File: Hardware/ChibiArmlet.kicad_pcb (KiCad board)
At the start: 2 copper layers, 8 x 8 mm, 52 parts, among them Q2 MMBT2222, Q3 LED_RGB 5050

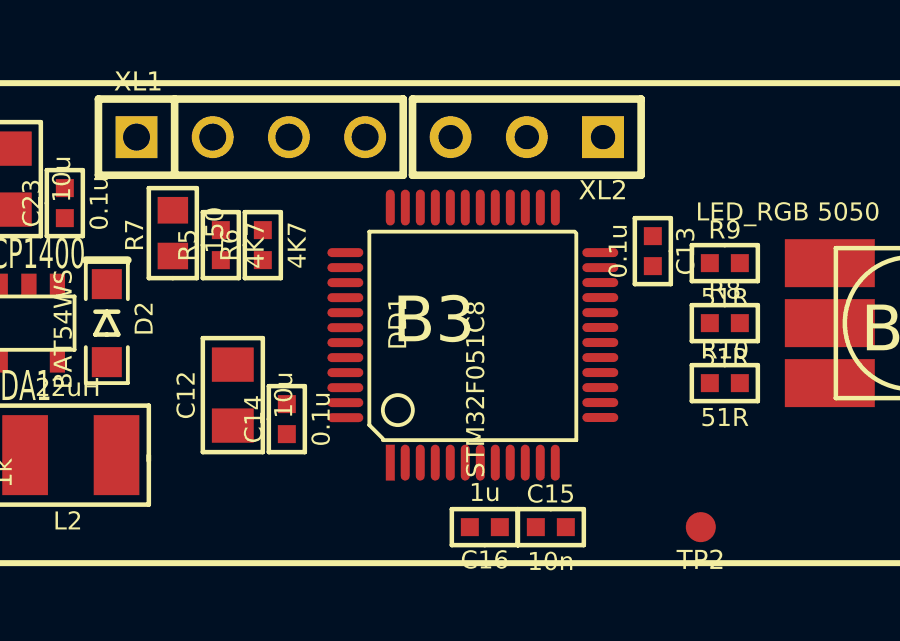
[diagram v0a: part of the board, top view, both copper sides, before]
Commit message: MCU replaced with stm32L100c6
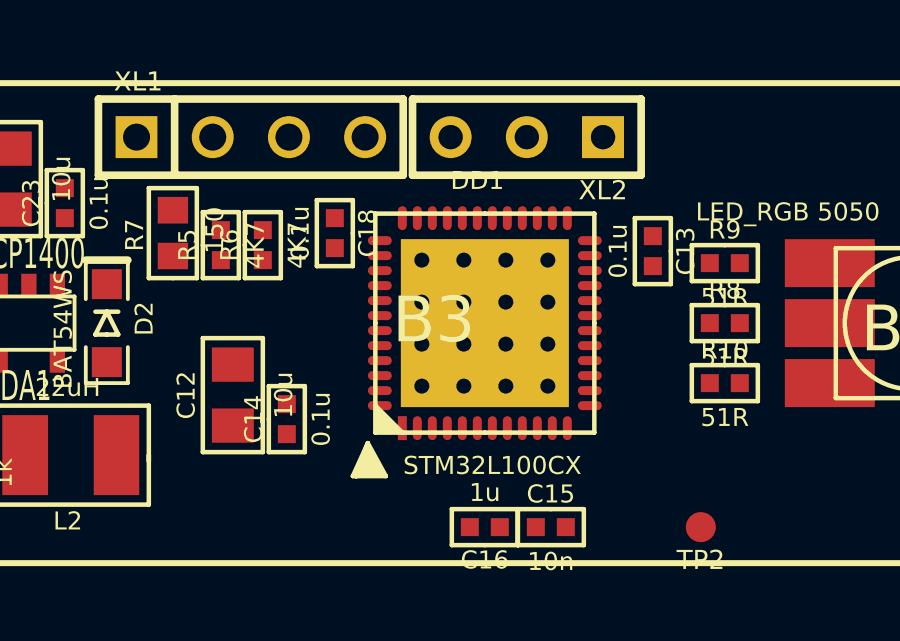
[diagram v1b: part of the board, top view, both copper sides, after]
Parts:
- added C18: 0.1u, CAP_0402, F.Cu at (197.0, 178.0)
- DD1: value STM32F051C8 -> STM32L100CX; footprint LQFP48 -> QFN48
- moved DD1 0.57 mm to (202.0, 181.0), turned to 0 degrees
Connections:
- DD1 pad 1: +3.3V -> (no net)
- DD1 pad 10: (no net) -> N-0000020
- DD1 pad 11: N-000001 (its old number) -> (no net)
- DD1 pad 21: (no net) -> /Buzzer
- DD1 pad 35: (no net) -> GND
- DD1 pad 36: (no net) -> +3.3V
- DD1 pad 40: /GREEN_LED -> (no net)
- DD1 pad 41: /PeriphPwr -> /GREEN_LED
- DD1 pad 42: /P_SCL -> (no net)
- DD1 pad 43: /P_SDA -> /PeriphPwr
- DD1 pad 45: /Buzzer -> /P_SCL
- DD1 pad 46: (no net) -> /P_SDA
- R1 pad 1: N-000001 (its old number) -> N-0000020

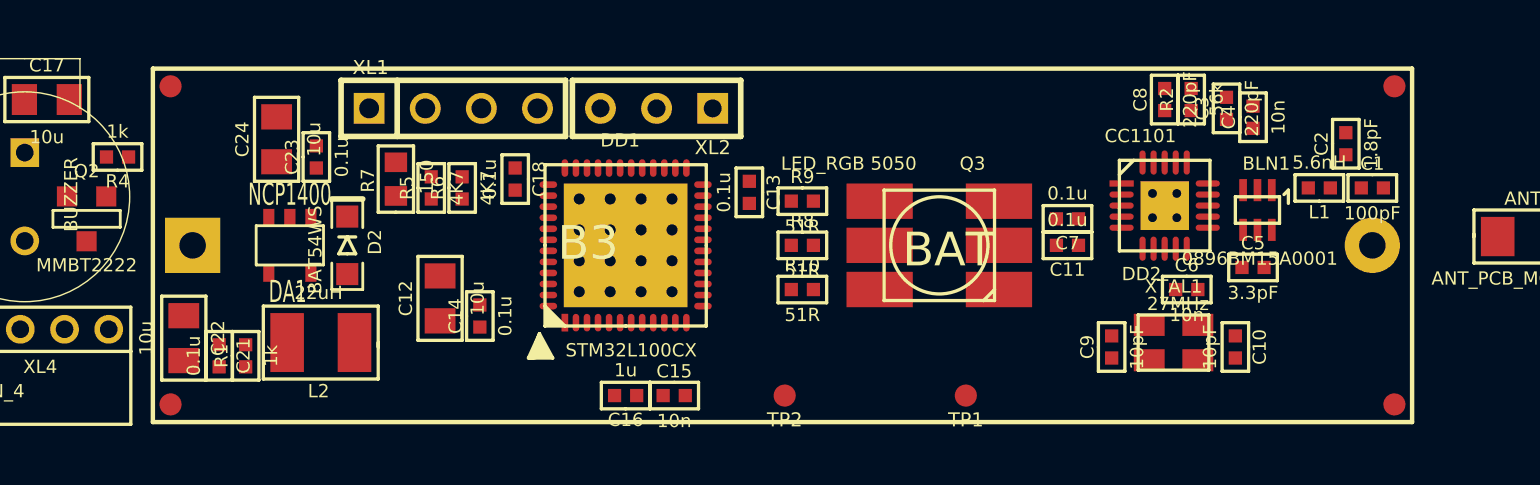
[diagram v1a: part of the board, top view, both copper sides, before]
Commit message: Again, buttons and display added.
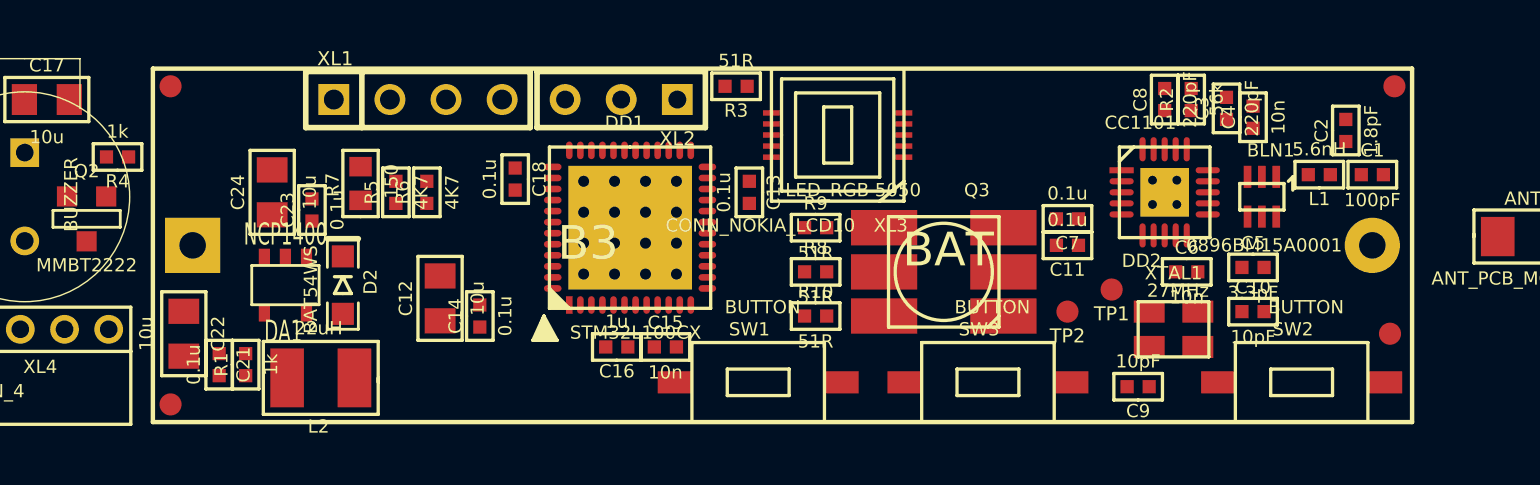
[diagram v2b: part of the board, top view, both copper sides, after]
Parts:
- added R3: 51R, RES_0402, F.Cu at (207.0, 173.8)
- added SW1: BUTTON, BUTTON_IT1181A, F.Cu at (208.0, 187.2)
- added SW2: BUTTON, BUTTON_IT1181A, F.Cu at (232.6, 187.2)
- added SW3: BUTTON, BUTTON_IT1181A, F.Cu at (218.4, 187.2)
- added XL3: CONN_NOKIA_LCD10, CONN_NOKIA_LCD, F.Cu at (211.6, 176.0)
- moved TP2 13.4 mm to (222.0, 184.0)
- moved TP1 8.16 mm to (224.0, 183.0)
- moved RP1 3.21 mm to (236.6, 185.0)
- moved C23 2.41 mm to (187.8, 179.4)
- moved C24 2.41 mm to (186.0, 178.6)
- moved C16 2.24 mm to (201.6, 185.6)
- moved C15 2.24 mm to (203.8, 185.6)
- moved C9 2.16 mm to (225.2, 187.4), turned to 180 degrees
- moved D2 1.81 mm to (189.2, 182.8)
- moved DA1 1.81 mm to (186.6, 182.8)
- moved C10 1.79 mm to (230.4, 184.0), turned to 0 degrees
- moved XL1 1.65 mm to (192.6, 174.4)
- moved XL2 1.65 mm to (201.8, 174.4)
- moved R5 1.61 mm to (191.6, 178.6)
- moved R6 1.61 mm to (193.0, 178.6)
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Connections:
- DD1 pad 11: (no net) -> /BTN1
- DD1 pad 20: (no net) -> /BTN2
- DD1 pad 21: /Buzzer -> /LCD_SDA
- DD1 pad 22: (no net) -> /LCD_XRES
- DD1 pad 25: (no net) -> /LCD_SCLK
- DD1 pad 26: (no net) -> /LCD_XCS
- DD1 pad 27: (no net) -> /LCD_BCKLT
- DD1 pad 28: (no net) -> /BTN3
- DD1 pad 39: (no net) -> /Buzzer

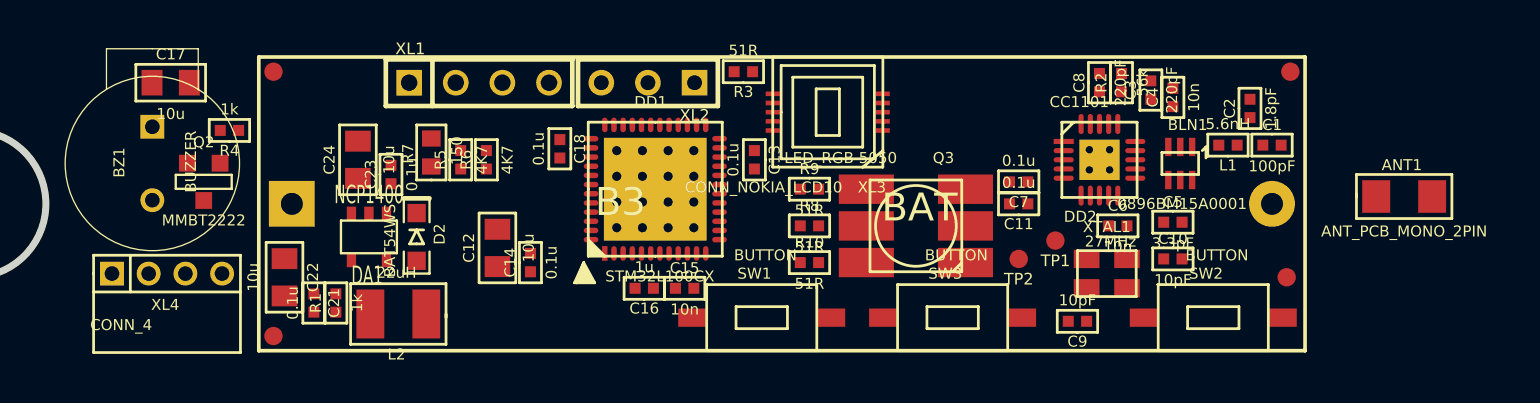
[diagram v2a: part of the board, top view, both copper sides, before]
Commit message: PCB routed save antenna. Quartz added.
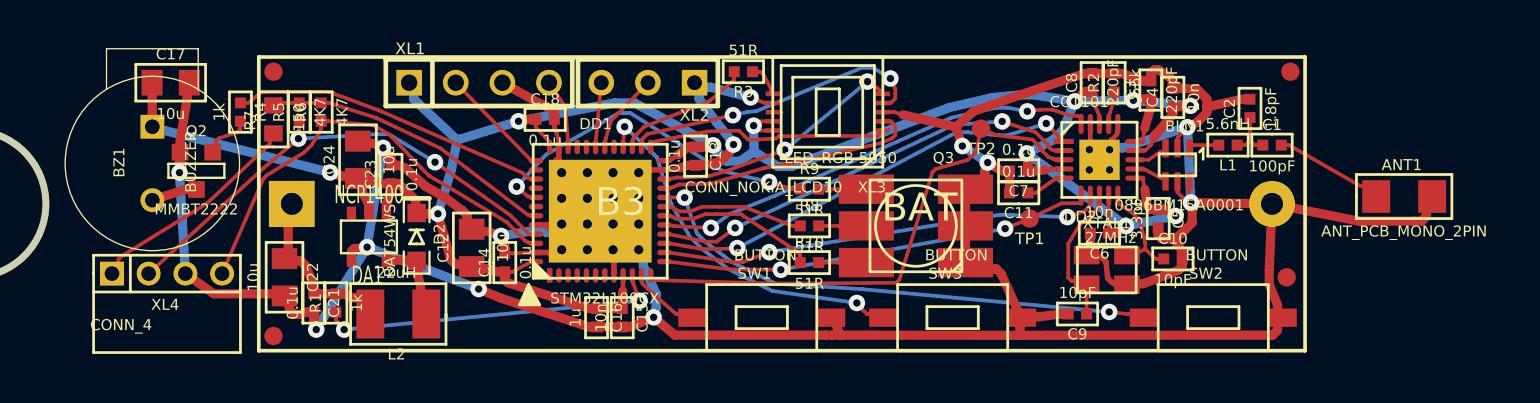
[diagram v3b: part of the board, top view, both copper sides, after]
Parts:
- moved R6 9.37 mm to (184.0, 176.0)
- moved R5 9.18 mm to (182.8, 176.0)
- moved R7 8.79 mm to (181.4, 176.4)
- moved TP2 7.39 mm to (219.9, 176.9)
- moved C15 3.76 mm to (200.4, 187.2), turned to 270 degrees
- moved DD1 3.23 mm to (199.2, 181.4)
- moved C13 3.21 mm to (204.4, 178.4)
- moved C16 3.05 mm to (199.0, 187.2), turned to 270 degrees
- moved TP1 1.84 mm to (222.6, 181.8)
- moved C18 1.79 mm to (196.2, 176.4), turned to 0 degrees
- moved C12 1.40 mm to (192.2, 183.4)
- moved C14 1.40 mm to (194.0, 184.2)
- moved R4 1.17 mm to (179.6, 176.0), turned to 270 degrees
- moved C6 1.08 mm to (226.4, 182.6), turned to 180 degrees
- moved C5 0.82 mm to (229.6, 181.8), turned to 270 degrees
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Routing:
- net GND: track 0.00 -> 224.0 mm, vias 0 -> 13
- net +3.3V: track 0.00 -> 133.9 mm, vias 0 -> 11
- net /CC_GDO2: track 0.00 -> 29.0 mm
- net /BTN2: track 0.00 -> 28.4 mm, vias 0 -> 2
- net /P_SCL: track 0.00 -> 26.6 mm, vias 0 -> 2
- net /CC_MOSI: track 0.00 -> 24.6 mm, vias 0 -> 2
- net /P_SDA: track 0.00 -> 24.3 mm
- net /CC_CS: track 0.00 -> 24.2 mm, vias 0 -> 2
- net /CC_SCK: track 0.00 -> 24.0 mm, vias 0 -> 2
- net /CC_MISO: track 0.00 -> 23.8 mm, vias 0 -> 2
- net /CC_GDO0: track 0.00 -> 23.6 mm, vias 0 -> 2
- net /BTN3: track 0.00 -> 20.0 mm, vias 0 -> 2
- net /GREEN_LED: track 0.00 -> 19.1 mm, vias 0 -> 2
- net N-0000025: track 0.00 -> 18.7 mm, vias 0 -> 2
- net /Buzzer: track 0.00 -> 17.3 mm
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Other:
- net class Default: clearance 0.254 -> 0.2; trace_width 0.254 -> 0.2; via_dia 0.889 -> 0.9; via_drill 0.635 -> 0.4
- net class Wide added: clearance 0.2, trace_width 0.5, via_dia 0.9, via_drill 0.4
- rule trace_clearance: 0.254 -> 0.2
- rule trace_min: 0.254 -> 0.1
- rule via_min_drill: 0.508 -> 0.3

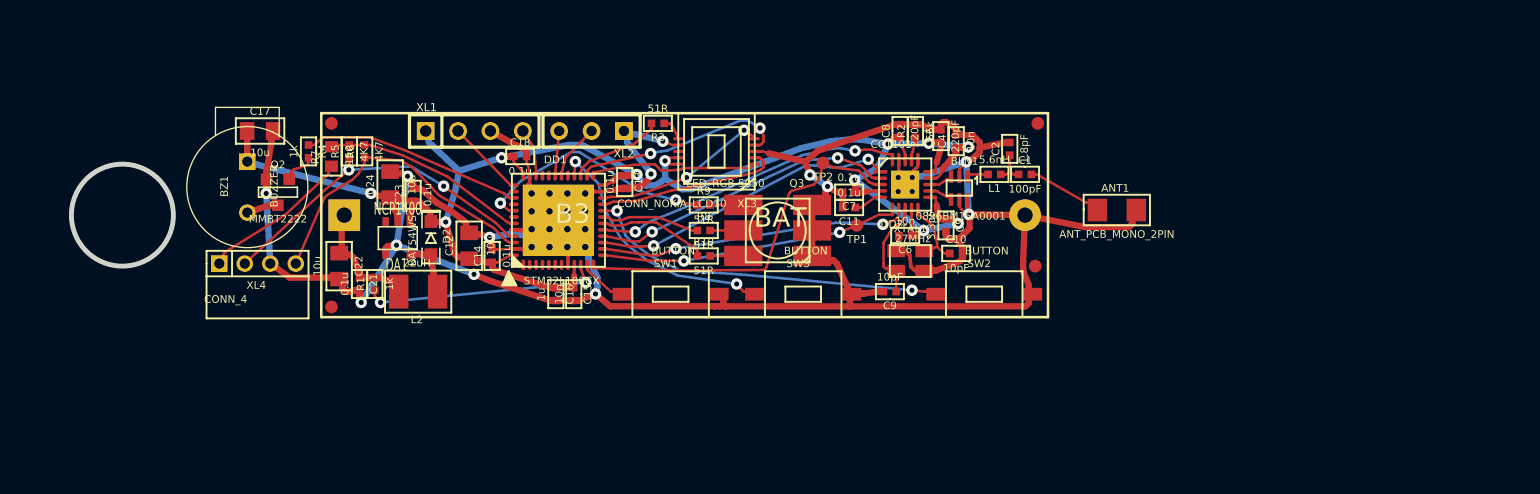
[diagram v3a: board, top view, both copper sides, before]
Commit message: + Antenna + Quartz 32768
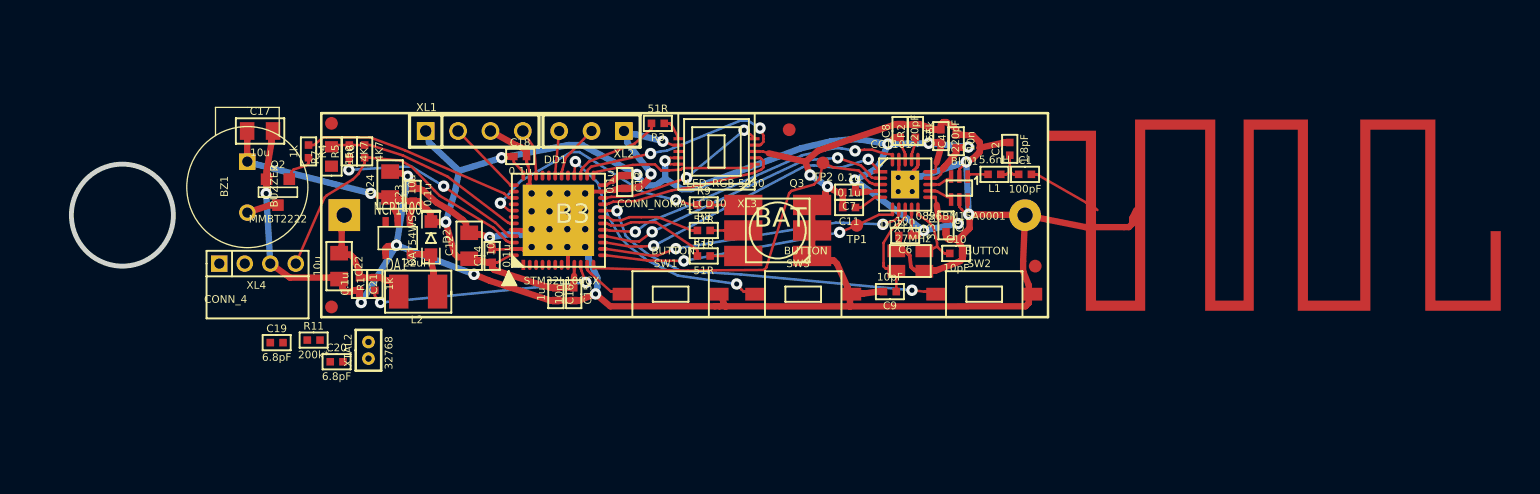
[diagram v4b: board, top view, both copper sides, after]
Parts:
- added C19: 6.8pF, CAP_0402, F.Cu at (177.1, 191.0)
- added C20: 6.8pF, CAP_0402, F.Cu at (181.8, 192.5)
- added R11: 200k*, RES_0402, F.Cu at (180.0, 190.8)
- added XTAL2: 32768, CRYSTAL_KX26_NOGND, F.Cu at (184.3, 191.6)
- ANT1: value ANT_PCB_MONO_2PIN -> ANT_PCB_MONO; footprint RES_1206 -> ANT_MEANDER868_16MM
- moved RP2 19.5 mm to (217.3, 174.3)
- moved ANT1 5.41 mm to (237.6, 181.0)
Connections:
- DD1 pad 3: (no net) -> N-0000032
- DD1 pad 4: (no net) -> N-0000034
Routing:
- net /PeriphPwr1: track 11.9 -> 0.00 mm
- net /P_SCL: track 26.6 -> 15.7 mm
- net GND: track 224.0 -> 223.3 mm
- net N-0000035: track 5.99 -> 6.70 mm

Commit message: Prototype sent to factory
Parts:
- removed C1: 100pF, CAP_0402
- moved R11 16.2 mm to (195.8, 187.2), turned to 270 degrees
- moved C19 15.2 mm to (192.0, 188.0), turned to 180 degrees
- moved C20 12.1 mm to (192.0, 186.0), turned to 180 degrees
- moved XTAL2 10.9 mm to (194.2, 187.0)
- moved SW2 7.00 mm to (225.6, 187.2)
- moved XTAL1 5.41 mm to (232.2, 184.2)
- moved C9 5.28 mm to (229.4, 183.8), turned to 90 degrees
- moved C10 4.40 mm to (234.8, 183.8), turned to 270 degrees
- moved C6 3.65 mm to (230.0, 182.0)
- moved C5 3.26 mm to (232.8, 181.2)
- moved Q3 3.23 mm to (219.4, 181.0)
- moved DD2 3.22 mm to (229.6, 178.2)
- moved C4 3.22 mm to (233.6, 174.8)
- moved BLN1 3.21 mm to (233.8, 178.5)
- moved R2 3.21 mm to (230.4, 174.2)
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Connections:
- ANT1 pad 1: N-0000035 (its old number) -> N-0000010
- C2 pad 1: N-000009 (its old number) -> N-0000010
- L1 pad 1: N-000009 (its old number) -> N-0000010
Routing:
- net GND: track 223.3 -> 302.4 mm, vias 13 -> 56
- net /PeriphPwr1: track 0.00 -> 11.9 mm
- net /P_SCL: track 15.7 -> 25.7 mm
- net N-0000035 (its old number): track 6.70 -> 0.00 mm
- net /BTN2: track 28.4 -> 21.9 mm
- net N-0000031: track 0.00 -> 4.45 mm
- net N-0000010: track 0.00 -> 4.32 mm
- net /CC_GDO0: track 23.6 -> 27.9 mm
- net /CC_CS: track 24.2 -> 28.5 mm
- net /CC_MOSI: track 24.6 -> 28.5 mm
- net /CC_SCK: track 24.0 -> 27.8 mm
- net /RED_LED: track 7.71 -> 11.5 mm
- net /CC_MISO: track 23.8 -> 27.5 mm
- net /CC_GDO2: track 29.0 -> 32.6 mm
- net /GREEN_LED: track 19.1 -> 22.6 mm
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- added copper zone on B.Cu, net GND
- added copper zone on F.Cu, net GND
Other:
- board size 8 x 8 mm -> 115 x 16 mm

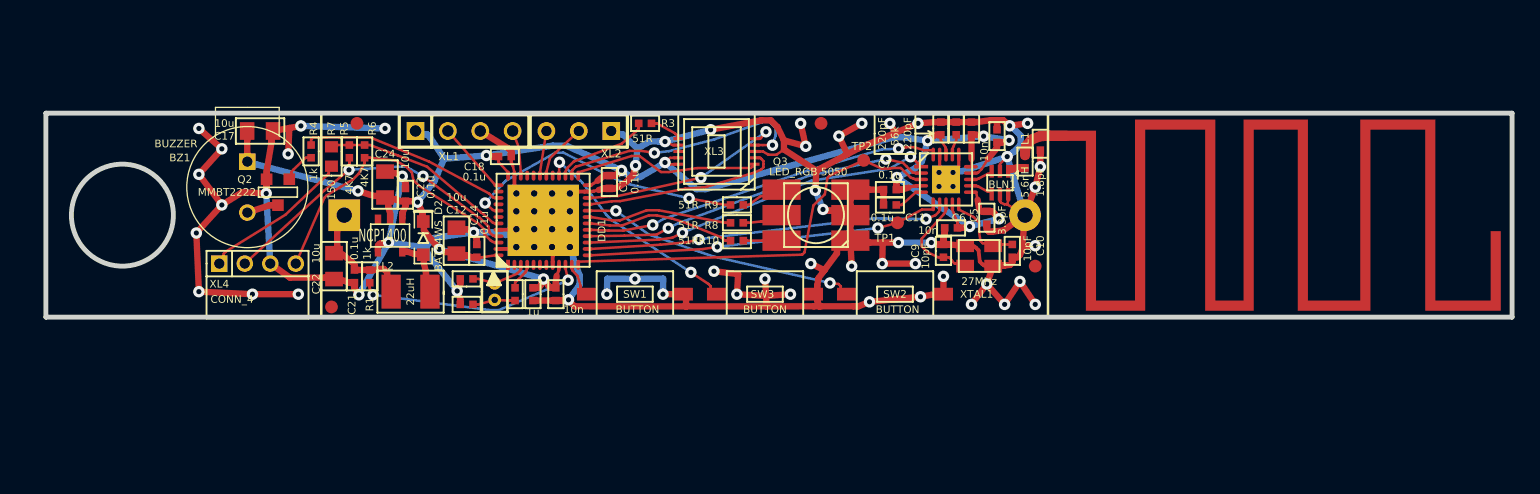
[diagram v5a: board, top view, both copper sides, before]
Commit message: + Vibro +Debug Pin * All R 0402 * 10u 0603
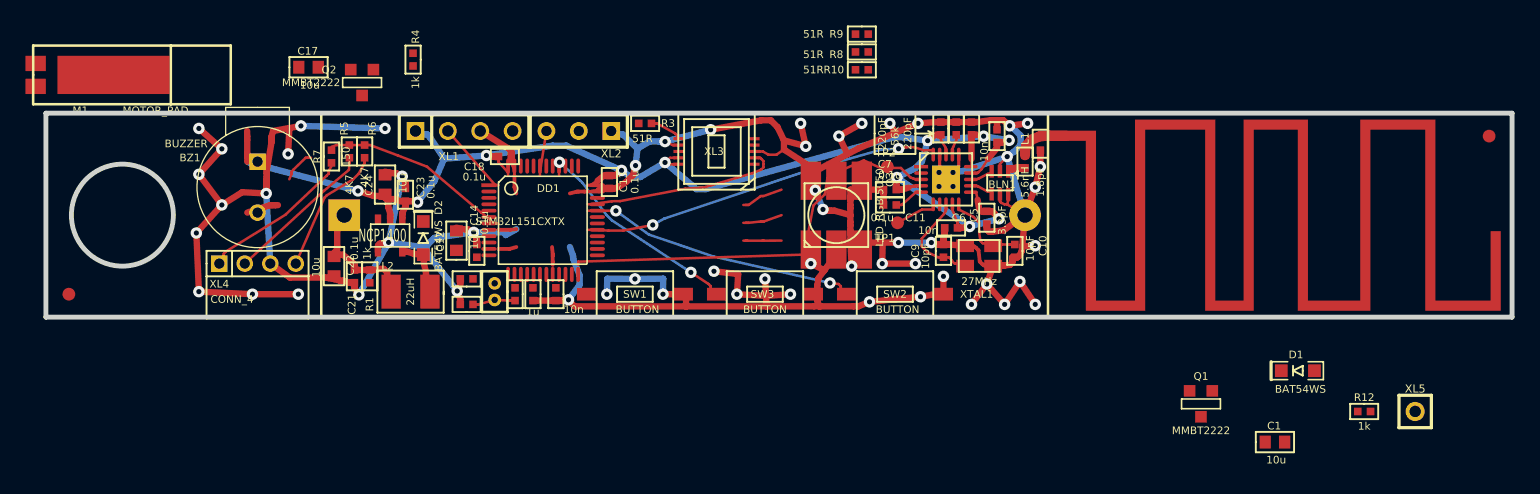
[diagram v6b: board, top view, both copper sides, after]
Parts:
- removed RP3, RP4: REFPOINT, REF_POINT_1MM
- added C1: 10u, CAP_0603, F.Cu at (255.4, 198.8)
- added D1: BAT54WS, DIODE_SOD323, F.Cu at (257.2, 193.2)
- added M1: MOTOR_PAD, MOTOR_KHN4NX, F.Cu at (158.0, 170.0)
- added Q1: MMBT2222, SOT23, F.Cu at (249.6, 195.8)
- added R12: 1k, RES_0402, F.Cu at (262.4, 196.4)
- added XL5: CONN_1, SIL-1, F.Cu at (266.4, 196.4)
- C12, C17, C22, C24: footprint CAP_0805 -> CAP_0603
- DD1: value STM32L100CX -> STM32L151CXTX; footprint QFN48 -> LQFP48
- R7: footprint RES_0603 -> RES_0402
- moved RP2 60.5 mm to (160.8, 187.2)
- moved RP1 37.0 mm to (272.2, 174.8)
- moved R10 16.6 mm to (223.0, 169.6)
- moved R8 16.6 mm to (223.0, 168.2)
- moved R9 16.6 mm to (223.0, 166.8)
- moved Q2 10.8 mm to (183.8, 170.6)
- moved R4 10.8 mm to (187.8, 168.8)
- moved C17 6.28 mm to (179.6, 169.4)
- moved TP2 1.92 mm to (225.0, 177.2)
- moved Q3 1.60 mm to (221.0, 181.0), turned to 270 degrees
- moved BZ1 0.80 mm to (175.6, 178.8)
- moved C10 0.20 mm to (235.0, 183.8)
- turned XTAL2 to 180 degrees
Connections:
- C19 pad 1: N-0000032 -> N-0000036
- C20 pad 1: N-0000031 -> N-0000044
- DD1 pad 1: (no net) -> +3.3V
- DD1 pad 27: /LCD_BCKLT -> /BTN3
- DD1 pad 28: /BTN3 -> /LCD_BCKLT
- DD1 pad 3: N-0000031 -> N-0000044
- DD1 pad 38: (no net) -> N-0000032
- DD1 pad 42: (no net) -> /Vibro
- R11 pad 2: N-0000032 -> N-0000036
- XTAL2 pad 1: N-0000031 -> N-0000036
- XTAL2 pad 2: N-0000032 -> N-0000044
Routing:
- net N-000001: track 3.00 -> 33.3 mm, vias 0 -> 8
- net /CC_CS: track 28.5 -> 0.00 mm, vias 2 -> 0
- net /CC_SCK: track 27.8 -> 0.00 mm, vias 2 -> 0
- net /CC_GDO2: track 32.6 -> 4.98 mm
- net /CC_MISO: track 27.5 -> 0.00 mm, vias 2 -> 0
- net /CC_GDO0: track 27.9 -> 3.47 mm, vias 2 -> 0
- net +3.3V: track 137.0 -> 112.9 mm, vias 13 -> 11
- net /GREEN_LED: track 22.6 -> 0.00 mm, vias 2 -> 0
- net (no net): track 0.00 -> 21.1 mm
- net /LCD_XCS: track 20.0 -> 0.00 mm, vias 2 -> 0
- net GND: track 302.4 -> 284.1 mm, vias 56 -> 48
- net N-0000027: track 18.1 -> 0.00 mm, vias 2 -> 0
- net /LCD_XRES: track 16.4 -> 0.00 mm, vias 2 -> 0
- net /Buzzer: track 16.3 -> 0.00 mm
- net /LCD_SCLK: track 14.9 -> 0.00 mm
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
